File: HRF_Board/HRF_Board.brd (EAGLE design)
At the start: 12.8 x 16.4 mm, 14 parts, among them U1 MAX30101EFD, Y1 ABS06-107-32.768KHZ-T

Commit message: Fully routed
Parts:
- removed C2, C3, C4: 1uF, SparkFun-Capacitors:0603
- removed C5: 100nF, SparkFun-Capacitors:0603
- removed R6: 10, SparkFun-Resistors:0603
- removed U$1: MAX32664_TQFN, MAX32664:MAX32664
- removed Y1: ABS06-107-32.768KHZ-T, ABS06-107-32.768KHZ-T:XTAL_ABS06-107-32.768KHZ-T
- moved R2 13.5 mm to (8.98, 7.44)
- moved R1 13.5 mm to (8.98, 5.96)
- moved C13 13.5 mm to (4.78, 10.6)
- moved R3 11.8 mm to (10.8, 10.3), turned to 90 degrees
- moved C1 11.0 mm to (9.30, 10.8), turned to 90 degrees
- moved U1 0.77 mm to (6.63, 8.56)
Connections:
- removed net MFIO: U$1.MFIO@1, U$1.MFIO@2, U$9.7
- removed net N$1: U$1.32KIN, Y1.2
- removed net N$3: U$1.32KOUT, Y1.1
- removed net N$4: C4.2, U$1.VCORE
- removed net N$7: C5.2, R6.2
- removed net RSTN: C5.1, U$1.RSTN, U$9.8
- removed net SCL_WMD: U$1.SLAVE_SCL, U$9.6
- removed net SDA_WMD: U$1.SLAVE_SDA, U$9.5
- net 1.8V: now also U$9.8; no longer C2.1, C3.1, U$1.VDD@1, U$1.VDD@2, U$9.4
- net 3.3V: now also U$9.6; no longer U$9.3
- net GND: now also U$9.2; no longer C2.2, C3.2, C4.1, R6.1, U$1.EP, U$1.VSS@1, U$1.VSS@2, U$1.VSS@3
- net HR_SCL: now also U$9.4; no longer U$1.SENSOR_SCL
- net HR_SDA: now also U$9.5; no longer U$1.SENSOR_SDA@1, U$1.SENSOR_SDA@2
- net INT: now also U$9.7; no longer U$1.HR_INT
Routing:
- net GND: track 0.00 -> 29.3 mm, vias 0 -> 3
- net 3.3V: track 0.00 -> 23.3 mm, vias 0 -> 1
- net INT: track 0.00 -> 16.6 mm, vias 0 -> 1
- net HR_SDA: track 0.00 -> 15.6 mm, vias 0 -> 2
- net HR_SCL: track 0.00 -> 13.0 mm, vias 0 -> 2
- net 1.8V: track 0.00 -> 12.0 mm, vias 0 -> 1
- removed copper zone on layer 1, net GND
- removed copper zone on layer 16, net GND
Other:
- board size 12.8 x 16.4 mm -> 11.8 x 13.6 mm
- board text added: "Jacob Bobson"
- board text added: "MARS HRFv1"

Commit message: DRC CHECK
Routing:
- net 3.3V: track 23.3 -> 24.0 mm
- net GND: track 29.3 -> 28.8 mm
- added copper zone on layer 1, net GND

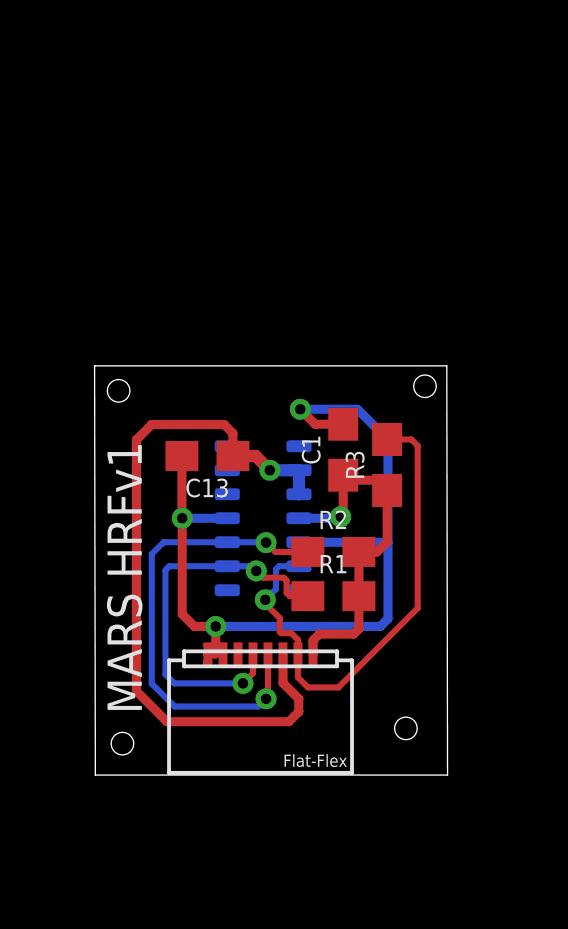
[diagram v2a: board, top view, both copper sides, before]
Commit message: Board outline fixes and tented vias
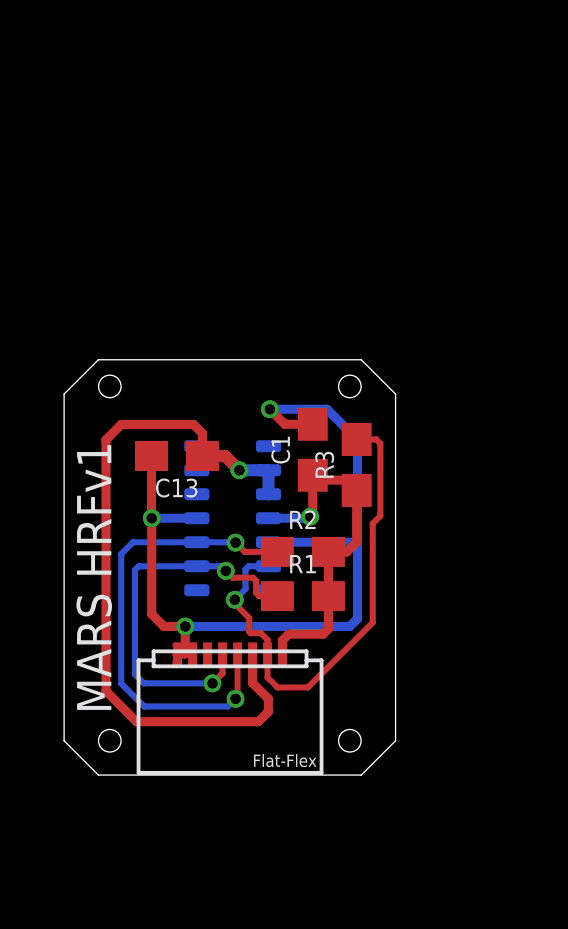
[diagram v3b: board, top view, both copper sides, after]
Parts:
- moved R1 1.02 mm to (7.96, 5.96)
- moved R2 1.02 mm to (7.96, 7.44)
- moved C1 1.02 mm to (8.29, 10.8)
- moved R3 1.02 mm to (9.75, 10.3)
- moved U$9 1.02 mm to (2.48, 0.07)
- moved U1 1.02 mm to (5.62, 8.56)
- moved C13 1.02 mm to (3.76, 10.6)
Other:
- board size 11.8 x 13.6 mm -> 11 x 13.8 mm
